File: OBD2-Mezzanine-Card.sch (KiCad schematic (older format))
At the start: 2 parts, among them P1 CONN_02X20, P2 CONN_02X20

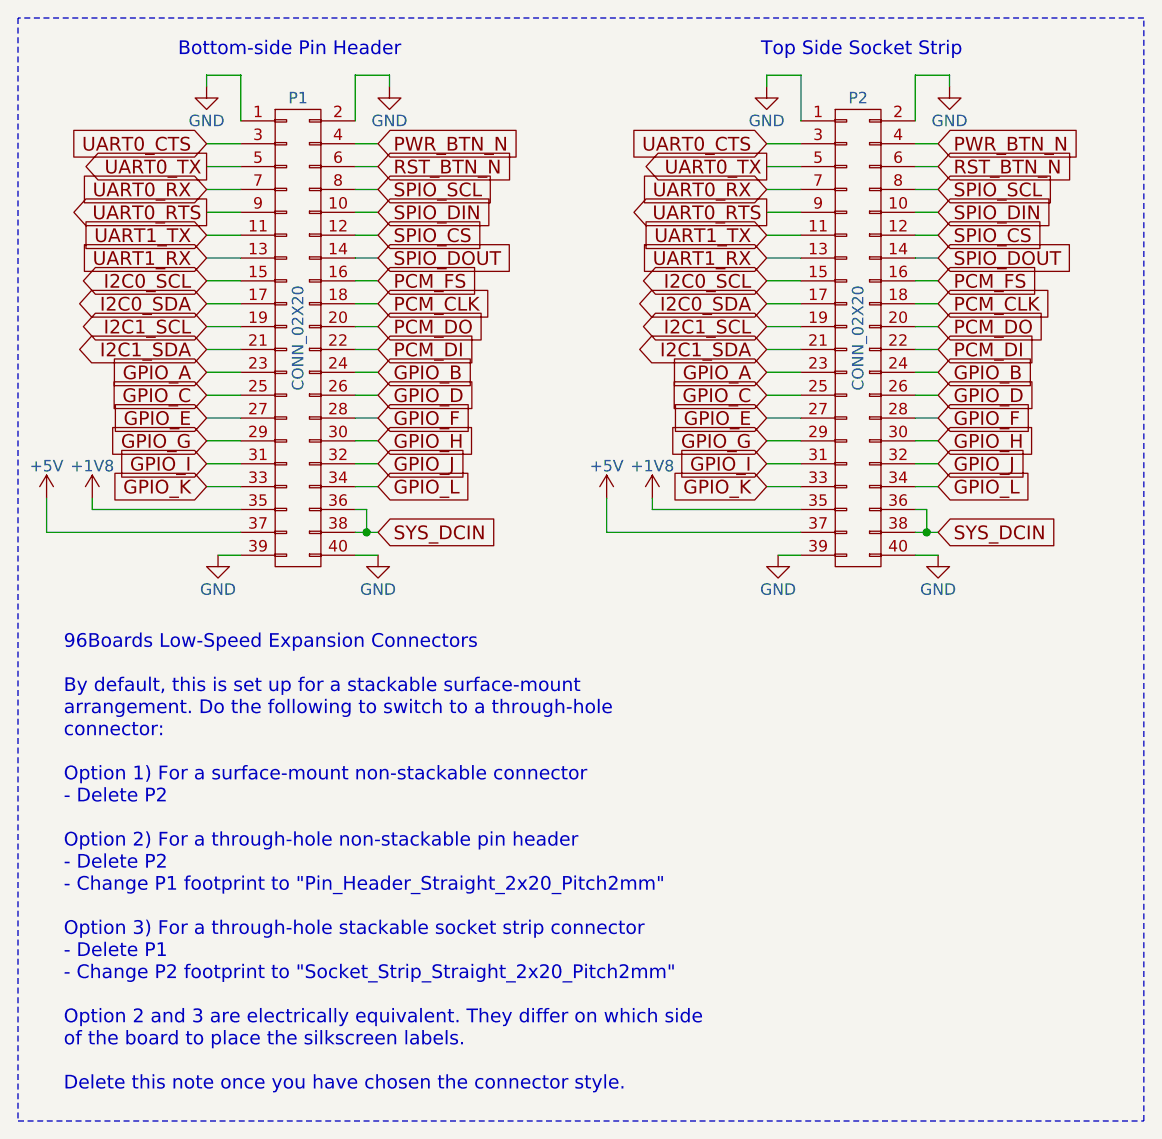
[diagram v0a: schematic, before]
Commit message: sch: Change to a through-hole non-stackable pin header
Signed-off-by: Alistair Francis <alistair@alistair23.me>
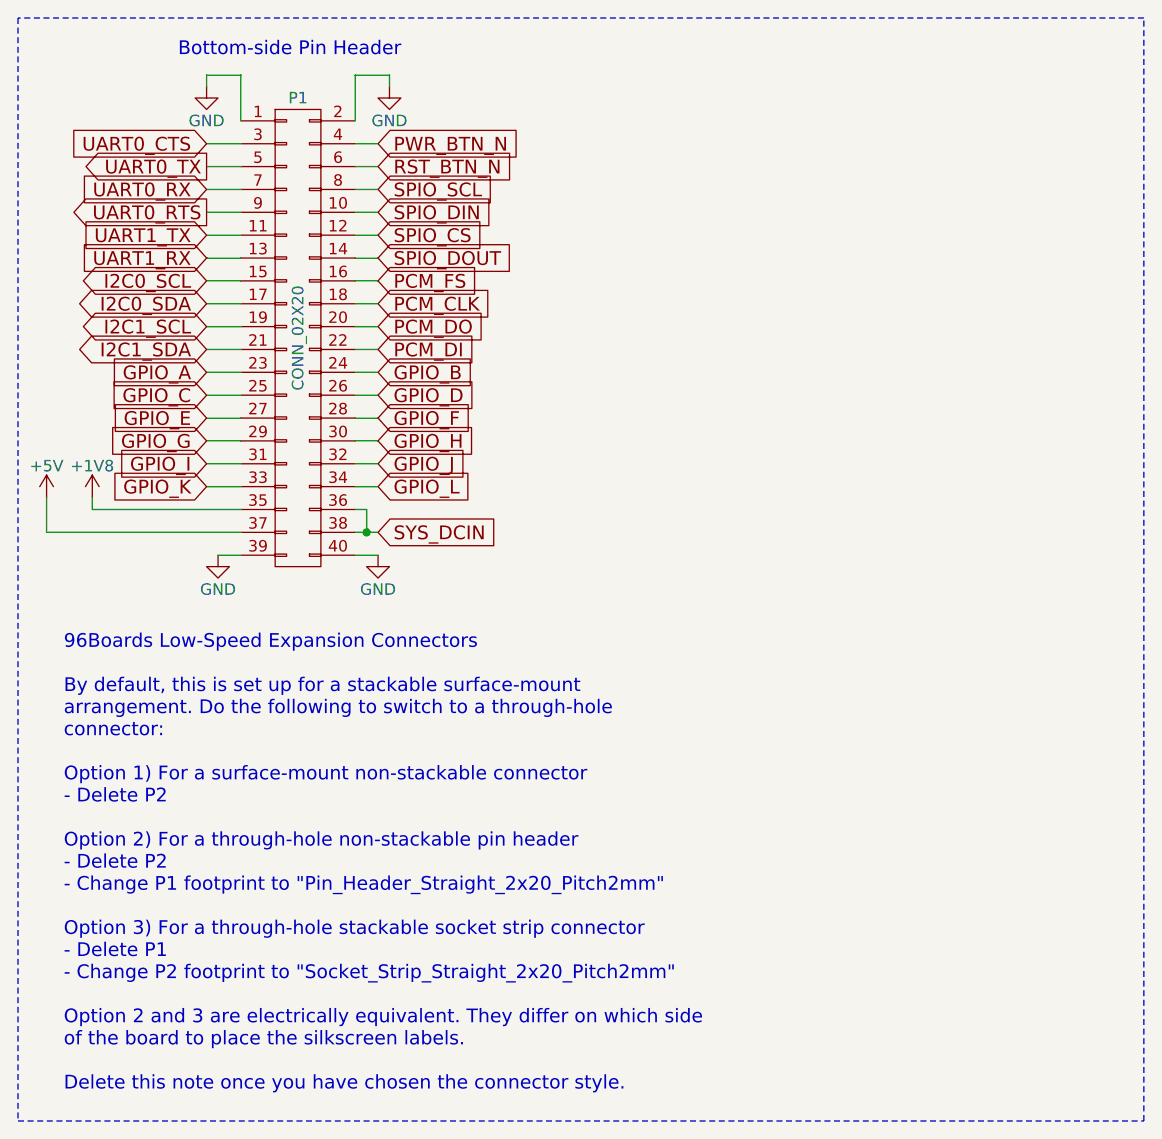
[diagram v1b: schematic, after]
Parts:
- removed P2: CONN_02X20, 96boards:Socket_Strip_SMD_2x20_Pitch2mm, symbol CONN_02X20
- P1: footprint 96boards:Pin_Header_SMD_2x20_Pitch2mm -> 96boards:Pin_Header_Straight_2x20_Pitch2mm
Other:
- note removed: "Top Side Socket Strip"

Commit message: sch: Delete Linaro notes
Signed-off-by: Alistair Francis <alistair@alistair23.me>
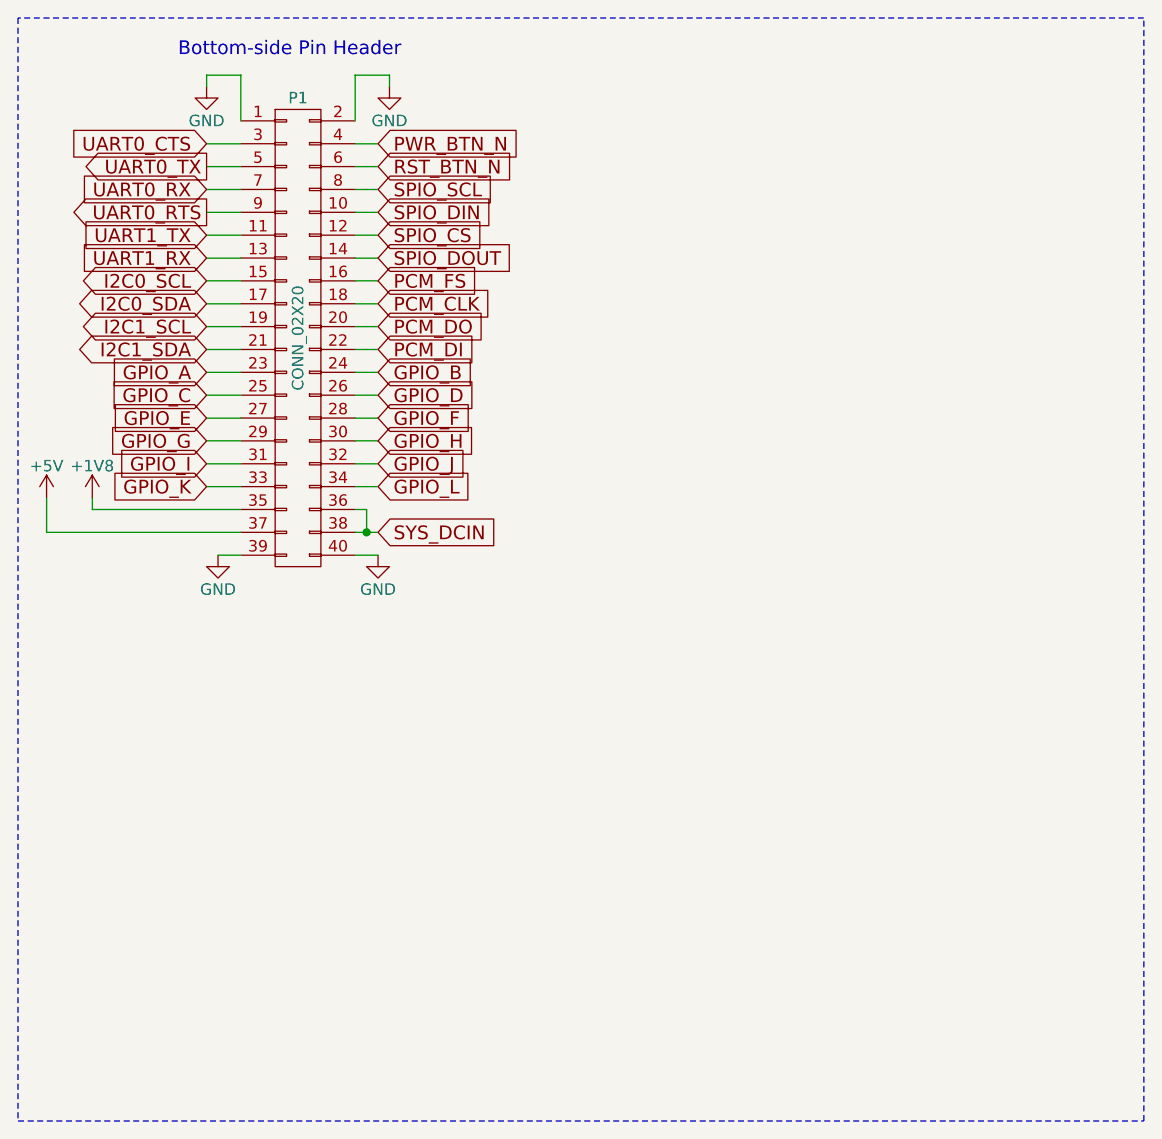
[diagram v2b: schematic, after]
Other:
- note removed: "96Boards Low-Speed Expansion Connectors\n\nBy default, this is set up for a stackable surface-mount\narrangement. Do the following to switch to a through-hole\nconnector:\n\nOption 1) For a surface-mount non-stackable connector\n- Delete P2\n\nOption 2) For a through-hole non-stackable pin header\n- Delete P2\n- Change P1 footprint to "Pin_Header_Straight_2x20_Pitch2mm"\n\nOption 3) For a through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"
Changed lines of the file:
@@
 Comment4 ""
 $EndDescr
-Text Notes 875  5350 0    60   ~ 0
-96Boards Low-Speed Expansion Connectors\n\nBy default, this is set up for a stackable surface-mount\narrangement. Do the following to switch to a through-hole\nconnector:\n\nOption 1) For a surface-mount non-stackable connector\n- Delete P2\n\nOption 2) For a through-hole non-stackable pin header\n- Delete P2\n- Change P1 footprint to "Pin_Header_Straight_2x20_Pitch2mm"\n\nOption 3) For a through-hole stackable socket strip connector\n- Delete P1\n- Change P2 footprint to "Socket_Strip_Straight_2x20_Pitch2mm"\n\nOption 2 and 3 are electrically equivalent. They differ on which side\nof the board to place the silkscreen labels.\n\nDelete this note once you have chosen the connector style.
 $Comp
 L GND #PWR07

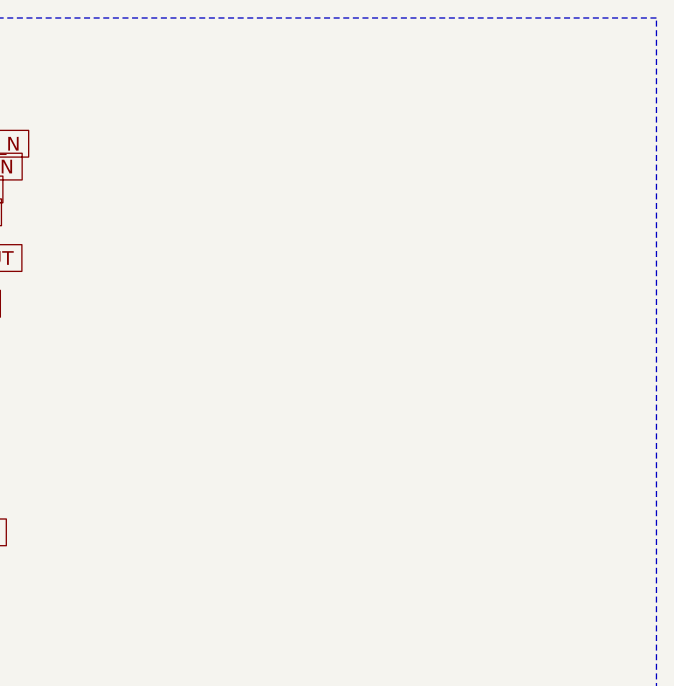
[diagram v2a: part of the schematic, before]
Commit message: lib: Add the ELM327 component
Signed-off-by: Alistair Francis <alistair@alistair23.me>
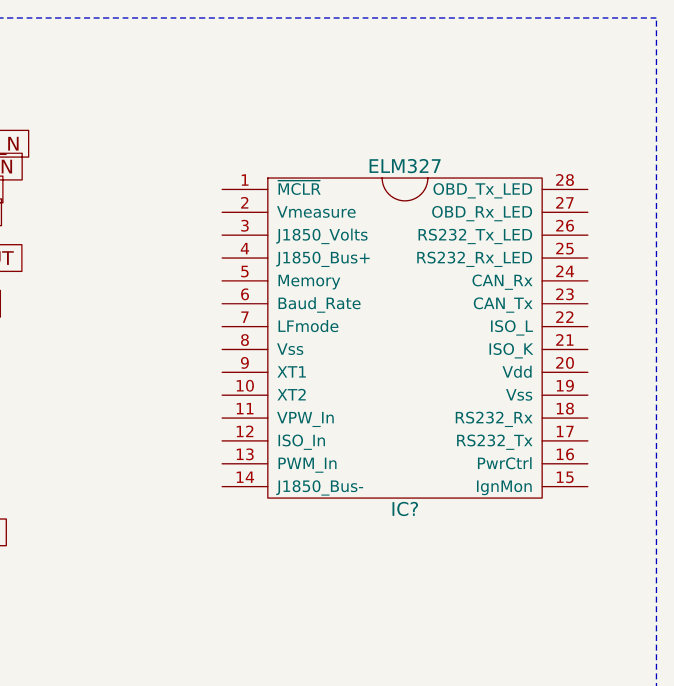
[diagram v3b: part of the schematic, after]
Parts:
- added IC?: ELM327, symbol ELM327
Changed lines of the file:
@@
 LIBS:valves
 LIBS:96boards
+LIBS:elm327
 LIBS:OBD2-Mezzanine-Card-cache
 EELAYER 25 0
@@
 Wire Notes Line
 	5600 650  675  650
+$Comp
+L ELM327 IC?
+U 1 1 5AA5E7D4
+P 4500 2050
+F 0 "IC?" H 4500 1300 60  0000 C CNN
+F 1 "ELM327" H 4500 2800 60  0000 C CNN
+F 2 "" H 4500 2800 60  0001 C CNN
+F 3 "" H 4500 2800 60  0001 C CNN
+	1    4500 2050
+	1    0    0    -1
+$EndComp
 $EndSCHEMATC
